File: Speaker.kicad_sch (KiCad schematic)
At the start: 25 parts, among them J1 AudioJack3_Ground, J2 Screw_Terminal_01x02, U1 NE5532

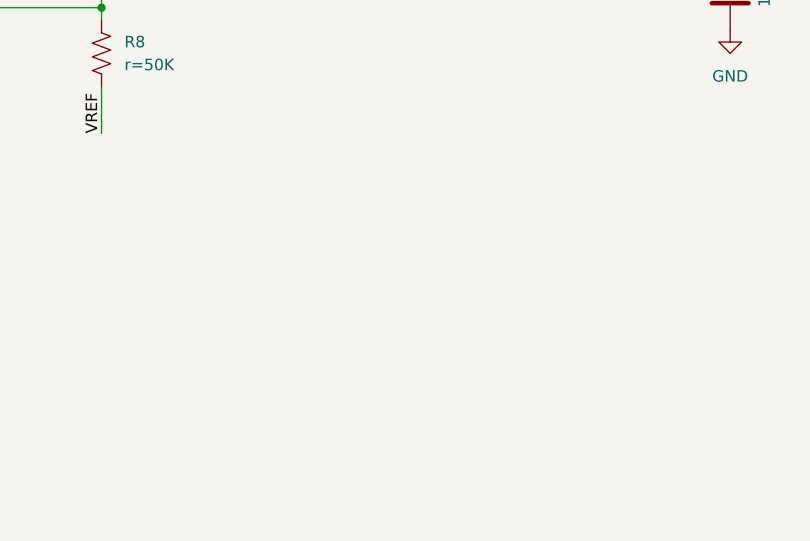
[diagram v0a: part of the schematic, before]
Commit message: Added power filtering for the NE5532
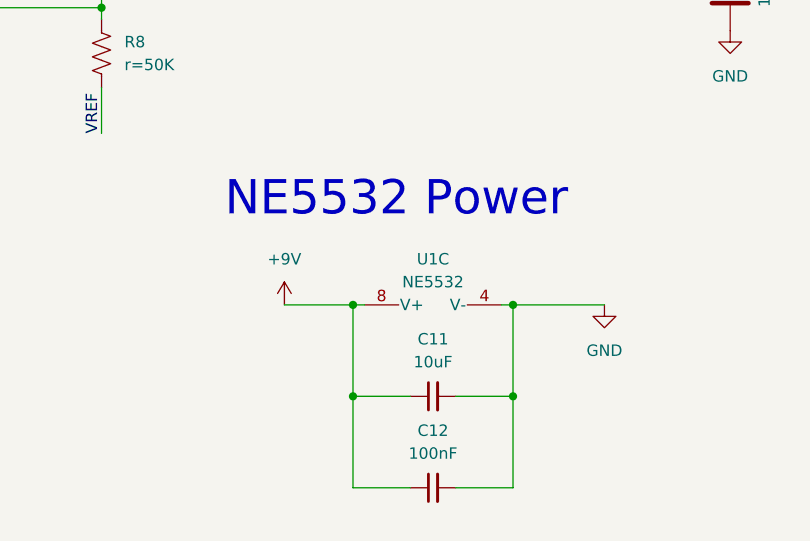
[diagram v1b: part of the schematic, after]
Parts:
- added C11: 10uF, symbol Device:C_Small
- added C12: 100nF, symbol Device:C_Small
- added unit 3 of U1
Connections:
- net +9V: now also C11.1, C12.1, U1.8 (V+)
- net GND: now also C11.2, C12.2, U1.4 (V-)
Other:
- note added: "NE5532 Power"

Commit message: Created PCB
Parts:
- added J3: Barrel_Jack_MountingPin, Connector_BarrelJack:BarrelJack_Horizontal, symbol Connector:Barrel_Jack_MountingPin
- added R8: ${SIM.PARAMS}, Resistor_THT:R_Axial_DIN0918_L18.0mm_D9.0mm_P22.86mm_Horizontal, symbol Device:R_US
- C1: renamed from C9; footprint (none) -> Capacitor_THT:C_Radial_D6.3mm_H5.0mm_P2.50mm
- C10: renamed from C7; footprint Capacitor_THT:C_Disc_D5.0mm_W2.5mm_P2.50mm -> Capacitor_THT:C_Radial_D6.3mm_H5.0mm_P2.50mm
- C11: footprint (none) -> Capacitor_THT:C_Radial_D6.3mm_H5.0mm_P2.50mm
- C12: footprint (none) -> Capacitor_THT:C_Disc_D3.0mm_W1.6mm_P2.50mm
- C2: renamed from C1; footprint Capacitor_THT:C_Disc_D5.0mm_W2.5mm_P2.50mm -> Capacitor_THT:C_Disc_D3.0mm_W1.6mm_P2.50mm
- C3: renamed from C10; footprint (none) -> Capacitor_THT:C_Disc_D3.0mm_W1.6mm_P2.50mm
- C4: renamed from C3; footprint Capacitor_THT:C_Disc_D5.0mm_W2.5mm_P2.50mm -> Capacitor_THT:C_Disc_D3.0mm_W1.6mm_P2.50mm
- C5: renamed from C4; footprint Capacitor_THT:C_Disc_D5.0mm_W2.5mm_P2.50mm -> Capacitor_THT:C_Disc_D3.0mm_W1.6mm_P2.50mm
- C6: renamed from C2; footprint Capacitor_THT:C_Disc_D5.0mm_W2.5mm_P2.50mm -> Capacitor_THT:C_Disc_D3.0mm_W1.6mm_P2.50mm
- C8: renamed from C5; footprint Capacitor_THT:C_Disc_D5.0mm_W2.5mm_P2.50mm -> Capacitor_THT:C_Radial_D6.3mm_H5.0mm_P2.50mm
- C9: renamed from C6; footprint Capacitor_THT:C_Disc_D5.0mm_W2.5mm_P2.50mm -> Capacitor_THT:C_Radial_D6.3mm_H5.0mm_P2.50mm
- CR1: footprint PDIP-8_STM -> Package_DIP:CERDIP-8_W7.62mm_SideBrazed_Socket
- J1: value AudioJack3_Ground -> AudioJack3; symbol Connector_Audio:AudioJack3_Ground -> Connector_Audio:AudioJack3
- J2: footprint (none) -> TerminalBlock:TerminalBlock_MaiXu_MX126-5.0-02P_1x02_P5.00mm
- R9: renamed from R5; footprint Resistor_THT:R_Axial_DIN0204_L3.6mm_D1.6mm_P5.08mm_Horizontal -> Resistor_THT:R_Axial_DIN0918_L18.0mm_D9.0mm_P22.86mm_Horizontal
- renumbered C8 to C7, R8 to R10, R9 to R11, R11 to R12, R6 to R2, R10 to R4, R4 to R5, R7 to R6, R2 to R7
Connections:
- net +9V: now also J3.1
- net GND: now also J3.2, J3.3 (MountPin); no longer J1.G
- net at C7.1, J2.1 (Pin_1), R9.2: now also R8.2
- net at C9.1, R9.1: now also R8.1
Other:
- moved on the sheet: C7

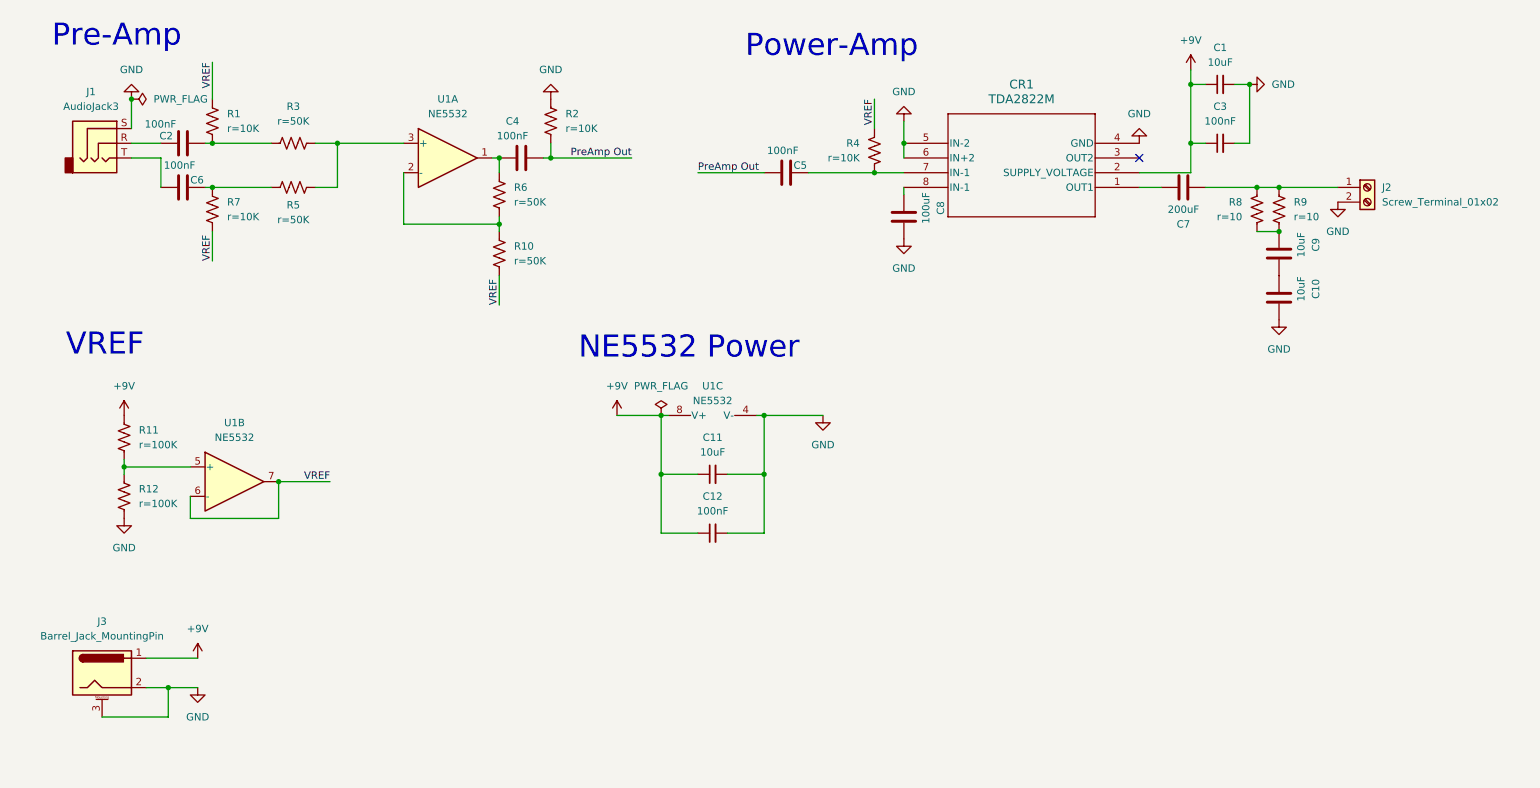
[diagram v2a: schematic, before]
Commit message: Replaced TDA2282 with LM386 and the barrel jack with a switching varient.
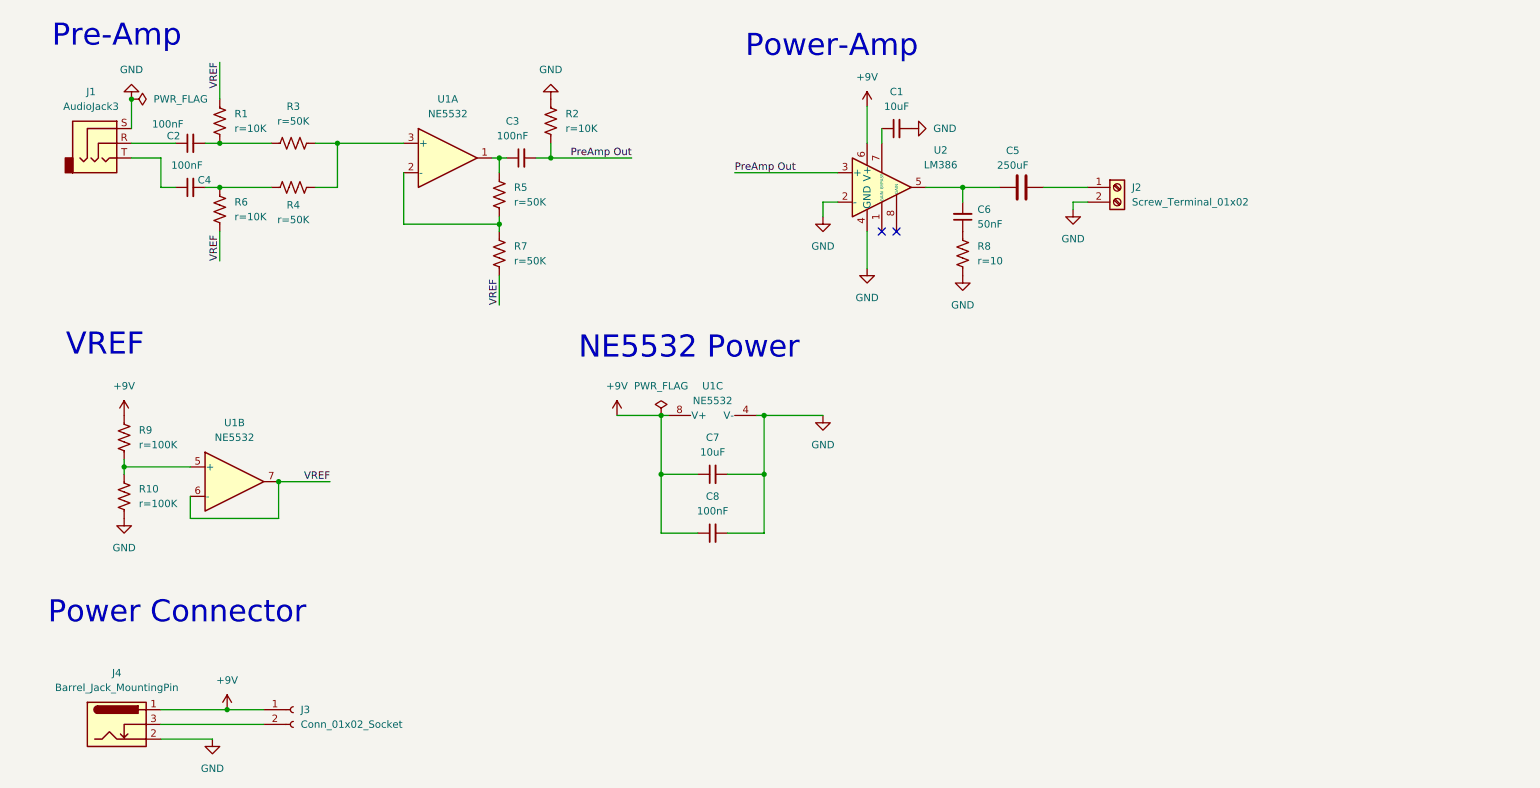
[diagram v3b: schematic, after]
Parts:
- removed C10, C9: 10uF, Capacitor_THT:C_Radial_D6.3mm_H5.0mm_P2.50mm, symbol Device:C
- removed C3: 100nF, Capacitor_THT:C_Disc_D3.0mm_W1.6mm_P2.50mm, symbol Device:C_Small
- removed C7: 200uF, Capacitor_THT:C_Disc_D5.0mm_W2.5mm_P2.50mm, symbol Device:C
- removed C8: 100uF, Capacitor_THT:C_Radial_D6.3mm_H5.0mm_P2.50mm, symbol Device:C
- removed CR1: TDA2822M, Package_DIP:CERDIP-8_W7.62mm_SideBrazed_Socket, symbol TDA2822M:TDA2822M
- removed R4: ${SIM.PARAMS}, Resistor_THT:R_Axial_DIN0204_L3.6mm_D1.6mm_P5.08mm_Horizontal, symbol Device:R_US
- removed R9: ${SIM.PARAMS}, Resistor_THT:R_Axial_DIN0918_L18.0mm_D9.0mm_P22.86mm_Horizontal, symbol Device:R_US
- added C6: 50nF, Capacitor_THT:C_Radial_D6.3mm_H5.0mm_P2.50mm, symbol Device:C_Small
- added J3: Conn_01x02_Socket, symbol Connector:Conn_01x02_Socket
- added U2: LM386, symbol Amplifier_Audio:LM386
- C2: symbol Device:C -> Device:C_Small
- C3: renamed from C4; symbol Device:C -> Device:C_Small
- C4: renamed from C6; symbol Device:C -> Device:C_Small
- C5: value 100nF -> 250uF
- J2: footprint TerminalBlock:TerminalBlock_MaiXu_MX126-5.0-02P_1x02_P5.00mm -> (none)
- J4: renamed from J3; symbol Connector:Barrel_Jack_MountingPin -> Connector:Barrel_Jack_Switch
- R8: footprint Resistor_THT:R_Axial_DIN0918_L18.0mm_D9.0mm_P22.86mm_Horizontal -> Resistor_THT:R_Axial_DIN0204_L3.6mm_D1.6mm_P5.08mm_Horizontal
- renumbered C11 to C7, C12 to C8, R12 to R10, R5 to R4, R6 to R5, R7 to R6, R10 to R7, R11 to R9
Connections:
- net +9V: now also J3.1 (Pin_1), U2.6 (V+); no longer C1.1
- net GND: now also R8.1, U2.2 (-), U2.4 (GND); no longer J4.3 (MountPin)
- net PreAmp Out: now also U2.3 (+); no longer C5.1
- net at C5.2: now also J2.1 (Pin_1)
- net at R8.2: now also C6.1; no longer J2.1 (Pin_1)
- new net: J3.2 (Pin_2), J4.3
- new net: C5.1, C6.2, U2.5
- new net: C1.1, U2.7 (BYPASS)
- no-connect marks 1 -> 2
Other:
- note added: "Power Connector"
- moved on the sheet: C2, C4, J4, R1, R6
